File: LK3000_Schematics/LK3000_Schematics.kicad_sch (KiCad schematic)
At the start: 59 parts, among them J1 Power In, J2 Keyboard-Display, J3 Power, J4 Cartridge, J5 Keyboard, J6 Power, SW1 A, SW10 T, SW11 U, SW12 V, SW13 E, SW14 F, SW15 G, SW16 H, SW17 N, SW18 O, SW19 P, SW2 B, SW20 Q, SW21 W, SW22 X, SW23 Y, SW24 Z, SW25 [?], SW26 [bs], SW27 R, SW28 I, SW29 [def], SW3 C, SW30 [stp], SW31 [sp], SW32 [f], SW33 Power, SW4 D, SW5 J, SW6 K, SW7 L, SW8 M, SW9 S, U1 74LS42, U2 74LS42, U3 CD4503BE, U4 7805

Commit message: Additional notes on schematic
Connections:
- net V_{IN}: now also J1.1, SW33.2 (B)
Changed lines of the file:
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@@
 		)
 	)
-	(text_box "Power Input (on Display Board)\nV_{OUT} and +5V must be bridged in the cartridge to enable the LK-3000 to power on.\nBattery is four AA NiCd cells connected in series."
+	(text_box "Power Input (on Display Board)\nV_{OUT} and +5V must be bridged in the cartridge to enable the LK-3000 to power on.\nBattery is four AA NiCd cells connected in series.\nV_{IN} is the input power from the PSU.\nV_{OUT} is the regulated +5V used by the system.\nV_{BATT} is the battery power source (charging/discharging)."
 		(exclude_from_sim no)
-		(at 26.67 172.72 0)
-		(size 88.9 60.96)
+		(at 26.67 166.37 0)
+		(size 88.9 67.31)
 		(margins 0.9525 0.9525 0.9525 0.9525)
 		(stroke
@@
 		(effects
 			(font
+				(size 1.27 1.27)
+			)
+			(justify left bottom)
+		)
+	)
+	(label "V_{IN}"
+		(at 54.61 194.31 0)
+		(effects
+			(font

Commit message: Updated schematic
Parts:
- C2: value C_Polarized -> 1µF
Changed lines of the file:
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@@
 	(title_block
 		(title "Nixdorf LK-3000 Personal Computer")
-		(date "21/SEP/2025")
-		(rev "WORK IN PROGRESS")
+		(date "23/SEP/2025")
+		(rev "A")
 		(company "Brett Hallen")
 		(comment 1 "www.youtube.com/@Brfff")
@@
 			)
 		)
-		(property "Value" "C_Polarized"
+		(property "Value" "1µF"
 			(at 85.09 35.9409 0)
 			(effects

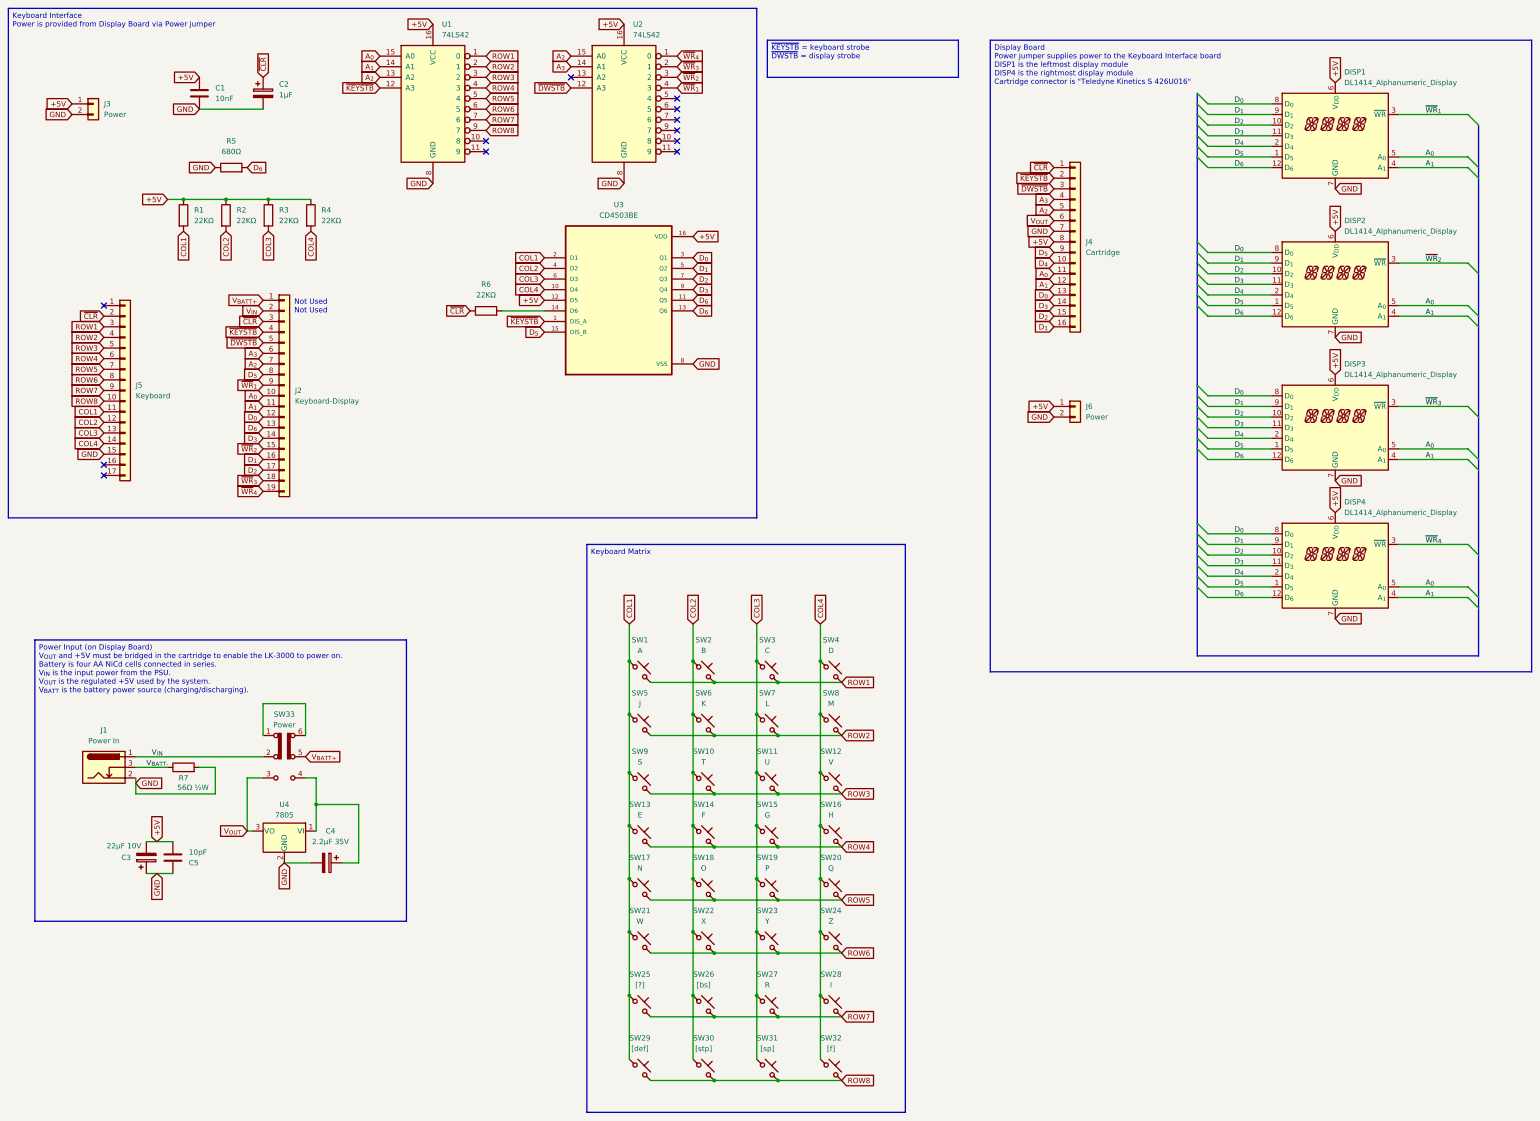
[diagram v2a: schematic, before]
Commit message: Schematic corrections
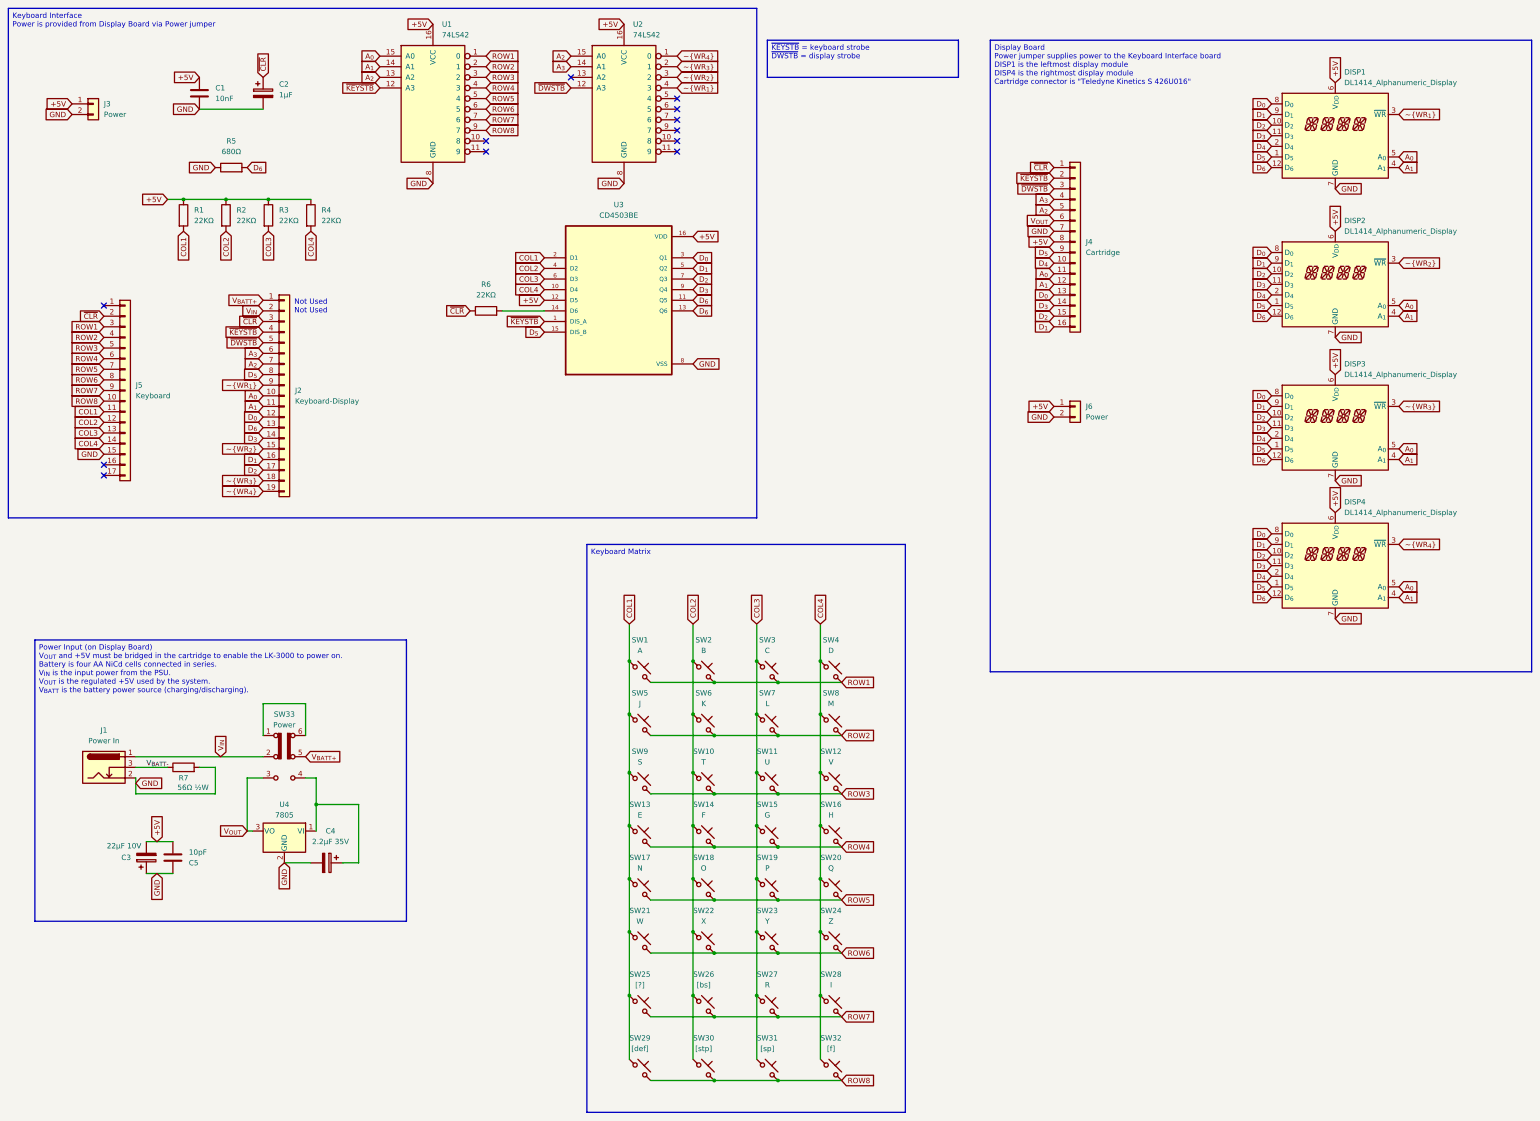
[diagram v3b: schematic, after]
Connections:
- net ~{WR}_{1} renamed ~{WR_{1}}
- net ~{WR}_{2} renamed ~{WR_{2}}
- net ~{WR}_{3} renamed ~{WR_{3}}
- net ~{WR}_{4} renamed ~{WR_{4}}

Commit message: Minor corrections to schematic
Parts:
- removed R2, R3, R4: 22KΩ, symbol Device:R
- removed R5: 680Ω, symbol Device:R
- added RN1: 22KΩ, Resistor_THT:R_Array_SIP5, symbol Device:R_Network04
- C1, C2: footprint (none) -> Capacitor_THT:C_Disc_D4.7mm_W2.5mm_P5.00mm
- J2: footprint (none) -> Connector_PinHeader_2.54mm:PinHeader_1x19_P2.54mm_Vertical
- J3, J6: footprint (none) -> Connector_PinHeader_2.54mm:PinHeader_1x02_P2.54mm_Vertical
- J4: footprint (none) -> Connector_PinHeader_2.54mm:PinHeader_1x16_P2.54mm_Vertical
- J5: footprint (none) -> Connector_PinHeader_2.54mm:PinHeader_1x17_P2.54mm_Vertical
- R1: value 22KΩ -> 680Ω; footprint (none) -> Resistor_THT:R_Axial_DIN0207_L6.3mm_D2.5mm_P10.16mm_Horizontal
- R6, R7: footprint (none) -> Resistor_THT:R_Axial_DIN0207_L6.3mm_D2.5mm_P10.16mm_Horizontal
- U1, U2: footprint (none) -> Package_DIP:DIP-16_W7.62mm
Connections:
- net +5V: now also R6.2, U3.14 (D6), RN1.1 (common); no longer R1.1
- net COL1: now also RN1.2 (R1); no longer R1.2
- net COL2: now also RN1.3 (R2)
- net COL3: now also RN1.4 (R3)
- net COL4: now also RN1.5 (R4)
- net D_{6}: now also R1.2
- net GND: now also R1.1, U2.13 (A2)
- no-connect marks 12 -> 11
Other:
- moved on the sheet: C1, C2, DISP3, DISP4, J2, J5, R6, U1, U2, U3
